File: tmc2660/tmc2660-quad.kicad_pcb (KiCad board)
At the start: 4 copper layers, 125 x 40 mm, 81 parts, among them J1 Power, J100 0R, J2 DataIn, J200 0R, J300 0R, J400 0R, M0 Mount, M1 Mount, M100 Mount, M101 Mount, M200 Mount, M201 Mount, M300 Mount, M301 Mount, M400 Mount, M401 Mount, P100 Motor, P200 Motor, P300 Motor, P400 Motor, U100 TMC2660, U200 TMC2660, U300 TMC2660, U400 TMC2660

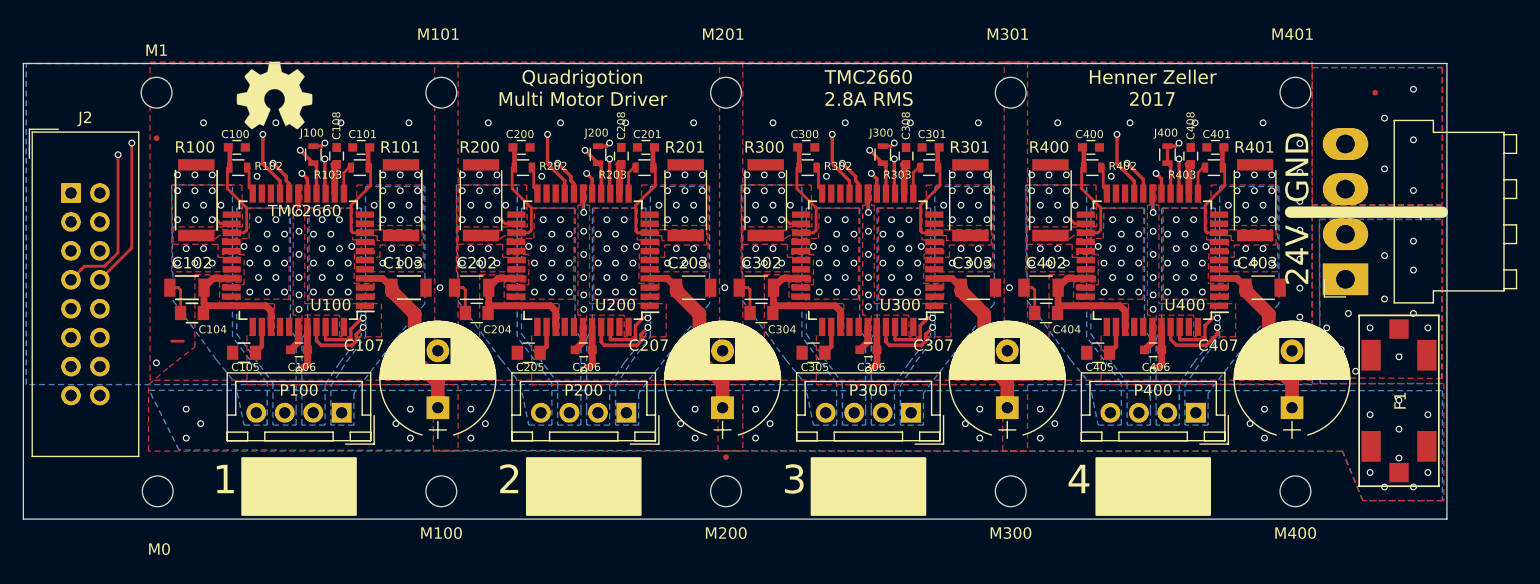
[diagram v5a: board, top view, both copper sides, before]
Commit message: Add digital connector legend. Round board corners.
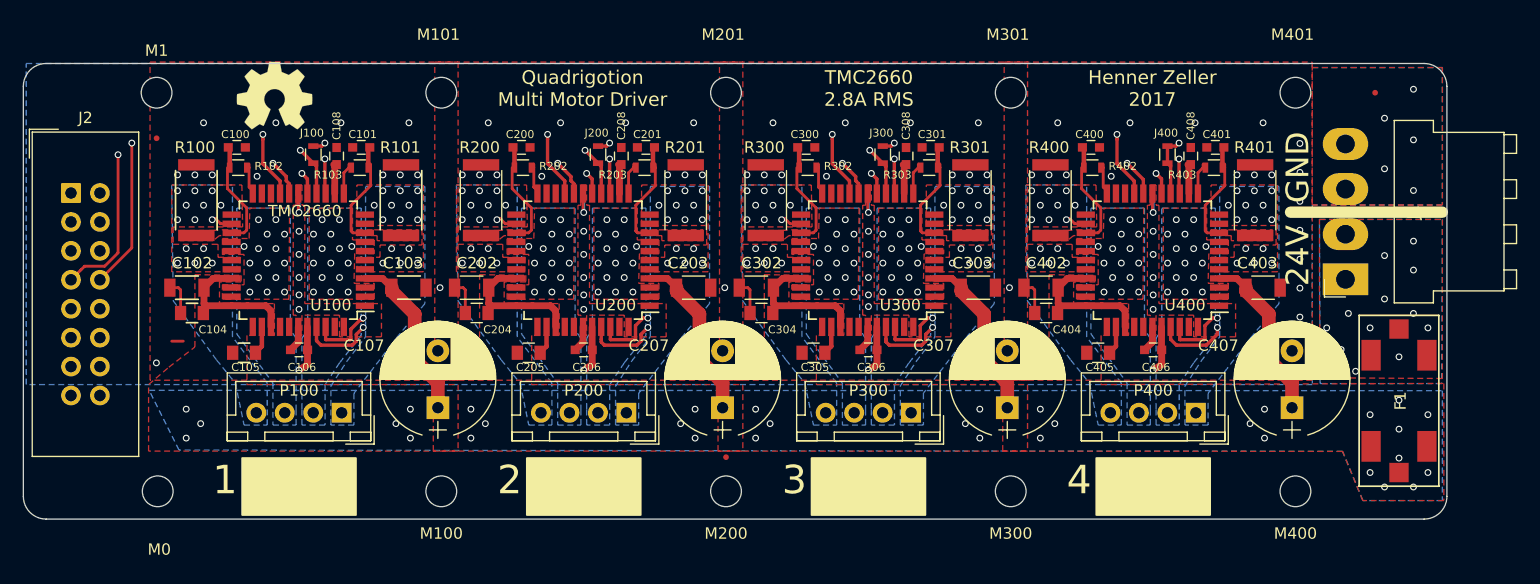
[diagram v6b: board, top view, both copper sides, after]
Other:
- outline, holes or cut-outs redrawn
- board text added: "D1"
- board text added: "D2"
- board text added: "D3"
- board text added: "D4"
- board text added: "MI"
- board text added: "MOSI"
- board text added: "N/C"
- board text added: "S1"
- board text added: "S2"
- board text added: "S3"
- board text added: "S4"
- board text added: "SCLK"
- board text added: "VCC"
- board text added: "~CS"
- board text added: "~EN"
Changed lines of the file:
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@@
   (general
     (thickness 1.6)
-    (drawings 24)
+    (drawings 44)
     (tracks 993)
     (zones 0)
@@
     )
   )
+  (gr_arc (start 182.614 50.514) (end 184.614 50.514) (angle -90) (layer Edge.Cuts) (width 0.1))
+  (gr_arc (start 61.614 50.514) (end 61.614 48.514) (angle -90) (layer Edge.Cuts) (width 0.1))
+  (gr_arc (start 182.614 86.519) (end 182.614 88.519) (angle -90) (layer Edge.Cuts) (width 0.1))
+  (gr_arc (start 61.614 86.519) (end 59.614 86.519) (angle -90) (layer Edge.Cuts) (width 0.1))
+  (gr_text VCC (at 68 59.8565) (layer B.SilkS)
+    (effects (font (size 1.2 1.2) (thickness 0.2)) (justify right mirror))
+  )
+  (gr_text N/C (at 68 62.3965) (layer B.SilkS)
+    (effects (font (size 1.2 1.2) (thickness 0.2)) (justify right mirror))
+  )
+  (gr_text SCLK (at 68 64.9365) (layer B.SilkS)
+    (effects (font (size 1.2 1.2) (thickness 0.2)) (justify right mirror))
+  )
+  (gr_text MOSI (at 68 67.4765) (layer B.SilkS)
+    (effects (font (size 1.2 1.2) (thickness 0.2)) (justify right mirror))
+  )
+  (gr_text D1 (at 68 70.0165) (layer B.SilkS)
+    (effects (font (size 1.2 1.2) (thickness 0.2)) (justify right mirror))
+  )
+  (gr_text D2 (at 68 72.5565) (layer B.SilkS)
+    (effects (font (size 1.2 1.2) (thickness 0.2)) (justify right mirror))
+  )
+  (gr_text D3 (at 68 75.0965) (layer B.SilkS)
+    (effects (font (size 1.2 1.2) (thickness 0.2)) (justify right mirror))
+  )
+  (gr_text D4 (at 68 77.6365) (layer B.SilkS)
+    (effects (font (size 1.2 1.2) (thickness 0.2)) (justify right mirror))
+  )
+  (gr_text S4 (at 62.5 77.6365) (layer B.SilkS)
+    (effects (font (size 1.2 1.2) (thickness 0.2)) (justify left mirror))
+  )
+  (gr_text S3 (at 62.5 75.0965) (layer B.SilkS)
+    (effects (font (size 1.2 1.2) (thickness 0.2)) (justify left mirror))
+  )
+  (gr_text S2 (at 62.5 72.5565) (layer B.SilkS)
+    (effects (font (size 1.2 1.2) (thickness 0.2)) (justify left mirror))
+  )
+  (gr_text S1 (at 62.5 70.0165) (layer B.SilkS)
+    (effects (font (size 1.2 1.2) (thickness 0.2)) (justify left mirror))
+  )
+  (gr_text MI (at 62.5 67.4765) (layer B.SilkS)
+    (effects (font (size 1.2 1.2) (thickness 0.2)) (justify left mirror))
+  )
+  (gr_text ~CS (at 62.5 64.9365) (layer B.SilkS)
+    (effects (font (size 1.2 1.2) (thickness 0.2)) (justify left mirror))
+  )
+  (gr_text ~EN (at 62.5 62.5235) (layer B.SilkS)
+    (effects (font (size 1.2 1.2) (thickness 0.2)) (justify left mirror))
+  )
+  (gr_text GND (at 62.9955 57.8245) (layer B.SilkS)
+    (effects (font (size 1.2 1.2) (thickness 0.2)) (justify mirror))
+  )
   (gr_text "TMC2660\n2.8A RMS" (at 133.8615 50.7125) (layer F.SilkS)
     (effects (font (size 1.2 1.2) (thickness 0.2)))
@@
     (effects (font (size 2.5 2.5) (thickness 0.5)) (justify right))
   )
-  (gr_line (start 184.614 48.514) (end 184.614 88.519) (layer Edge.Cuts) (width 0.1))
-  (gr_line (start 59.614 48.514) (end 184.614 48.514) (layer Edge.Cuts) (width 0.1))
-  (gr_line (start 59.614 88.519) (end 59.614 48.514) (layer Edge.Cuts) (width 0.1))
-  (gr_line (start 184.614 88.519) (end 59.614 88.519) (layer Edge.Cuts) (width 0.1))
+  (gr_line (start 184.614 50.514) (end 184.614 86.519) (layer Edge.Cuts) (width 0.1))
+  (gr_line (start 61.614 48.514) (end 182.614 48.514) (layer Edge.Cuts) (width 0.1))
+  (gr_line (start 59.614 86.519) (end 59.614 50.514) (layer Edge.Cuts) (width 0.1))
+  (gr_line (start 182.614 88.519) (end 61.614 88.519) (layer Edge.Cuts) (width 0.1))
   (via (at 181.677 50.776) (size 0.6) (drill 0.4) (layers F.Cu B.Cu) (net 1))
   (via (at 179.137 53.316) (size 0.6) (drill 0.4) (layers F.Cu B.Cu) (net 1))

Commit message: More easily fabricatable design rules: 0.8mm via/0.4mm drill.
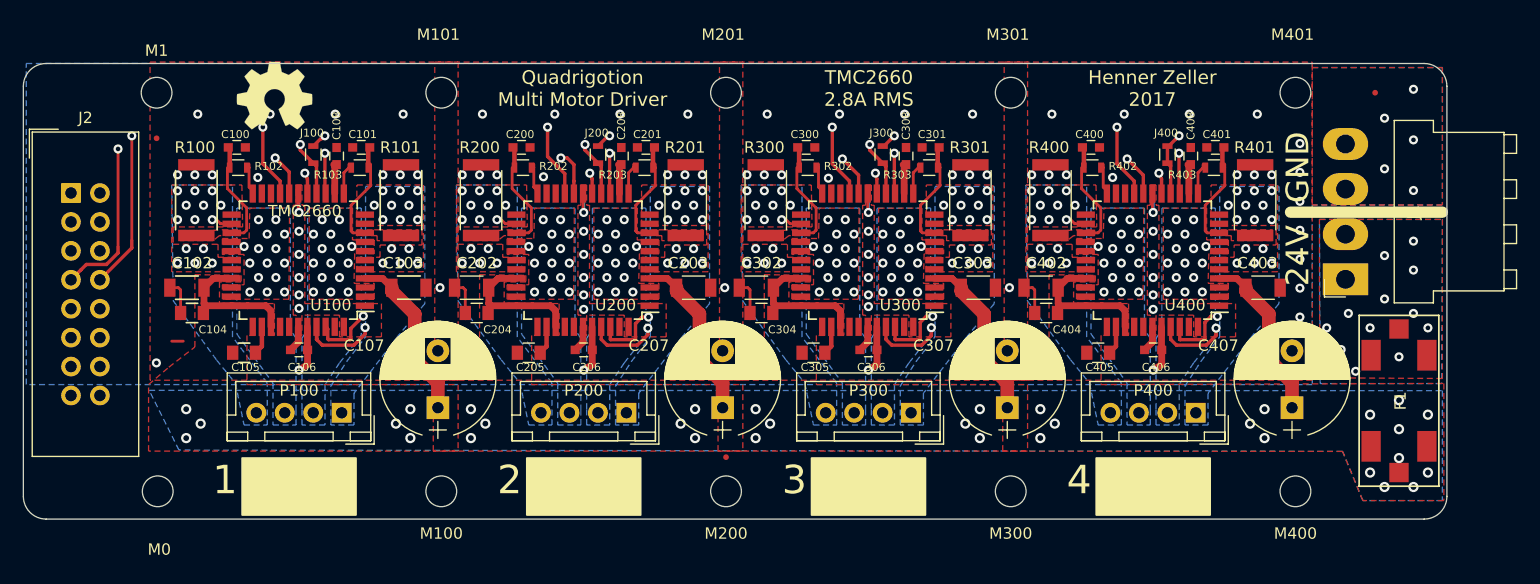
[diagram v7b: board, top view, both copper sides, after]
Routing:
- net ~ENABLE: track 120.1 -> 123.2 mm
- net GLOBAL_MOSI: track 113.9 -> 116.7 mm
- net CS: track 112.8 -> 114.9 mm
- net DIR1: track 30.9 -> 32.3 mm
- net DIR4: track 111.5 -> 110.4 mm
- net /TMC2660-400/MISO: track 34.9 -> 35.5 mm
- net /TMC2660-300/MISO: track 34.9 -> 35.5 mm
- net /TMC2660-200/MISO: track 34.9 -> 35.5 mm
- net GLOBAL_MISO: track 35.4 -> 35.9 mm
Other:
- net class Default: via_dia 0.6 -> 0.8
- net class MotPower: via_dia 0.6 -> 0.9; via_drill 0.4 -> 0.5
- rule via_min_drill: 0.3 -> 0.4
- rule via_min_size: 0.4 -> 0.7

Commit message: Move bottom silkscreen a little ouf of the way of vias.
o Also: larger vias in the general power input area.
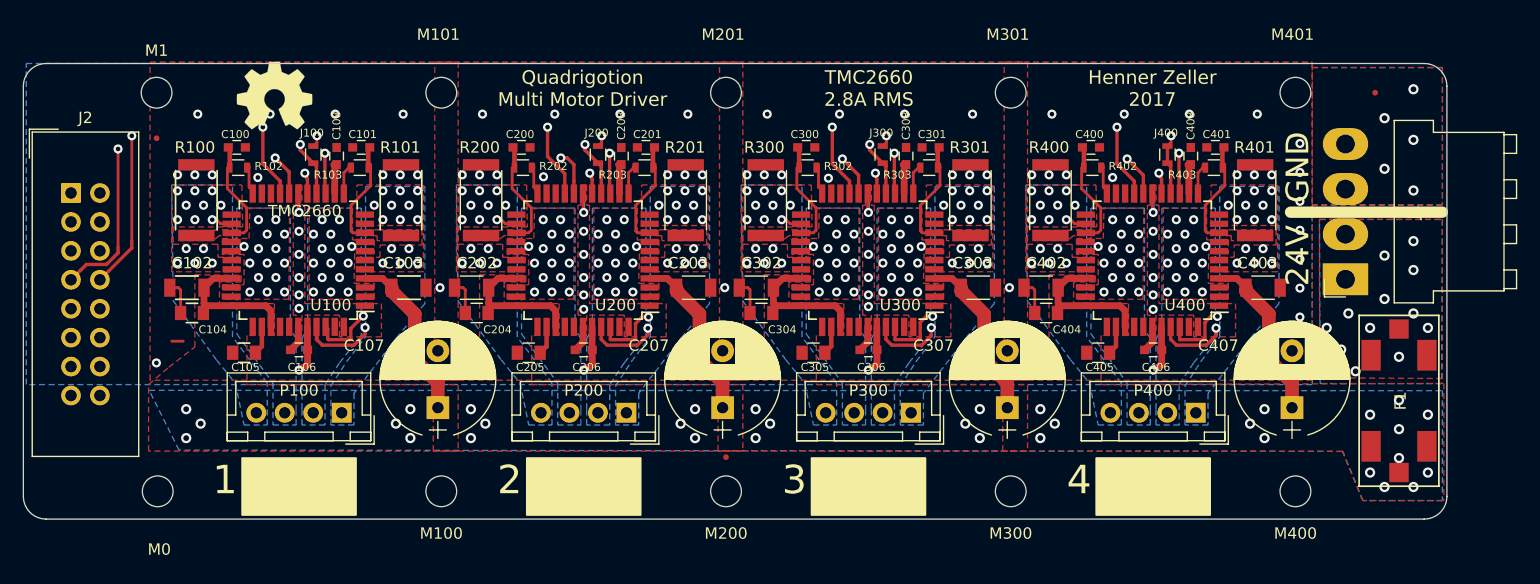
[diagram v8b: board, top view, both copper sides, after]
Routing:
- net GLOBAL_MOSI: track 116.7 -> 113.7 mm
